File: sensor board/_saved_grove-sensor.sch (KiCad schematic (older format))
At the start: 28 parts, among them P1 CONN_01X03, P2 CONN_01X03, P3 CONN_01X03, P4 CONN_01X04, Q1 PN2222A, U1 ADD8704, U2 SI1143, U3 Teensy_3.1

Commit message: Drew some footprints and PCB outline
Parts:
- C1, C2, C3: footprint (none) -> Capacitors_SMD:C_0603_HandSoldering
- D1, D2, D3: footprint (none) -> LEDs:LED-5MM
- P1, P2, P3: footprint (none) -> Pin_Headers:Pin_Header_Straight_1x03
- P4: footprint (none) -> Pin_Headers:Pin_Header_Straight_1x04
- Q1: footprint (none) -> TO_SOT_Packages_THT:TO-92_Horizontal1_Inline_Narrow_Oval
- R1, R10, R11, R12, R13, R14, R3, R4, R6, R7, R8, R9: footprint (none) -> Resistors_SMD:R_0603_HandSoldering
- R2, R5: footprint (none) -> Resistors_SMD:R_0402
- U2: footprint (none) -> SI1143:SI1143

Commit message: Added sensor mounting holes
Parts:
- removed P1, P2, P3: CONN_01X03, Pin_Headers:Pin_Header_Straight_1x03, symbol CONN_01X03
- removed P4: CONN_01X04, Pin_Headers:Pin_Header_Straight_1x04, symbol CONN_01X04
- removed Q1: PN2222A, TO_SOT_Packages_THT:TO-92_Horizontal1_Inline_Narrow_Oval, symbol PN2222A
- added C4: 10uF, Capacitors_SMD:C_0603_HandSoldering, symbol C
- added C5, C6: 0.1uF, Capacitors_SMD:C_0603_HandSoldering, symbol C
- added P1, P3, P4, P5, P6, P7, P8, P9: CONN_01X01, Pin_Headers:Pin_Header_Straight_1x01, symbol CONN_01X01
- added P2: CONN_01X06, Pin_Headers:Pin_Header_Straight_1x06, symbol CONN_01X06
- added Q1: Q_NPN_BEC, TO_SOT_Packages_SMD:SOT-23, symbol Q_NPN_BEC
- added R21, R22, R25: 0, Resistors_SMD:R_0603_HandSoldering, symbol R
- added R23, R24, R26: 10k, Resistors_SMD:R_0603_HandSoldering, symbol R
- added U4: MCP1700, TO_SOT_Packages_SMD:SOT-23, symbol MCP1700
- added U5, U6: WS2812B, LEDs:LED_WS2812B-PLCC4, symbol WS2812B
- D1, D2, D3: footprint LEDs:LED-5MM -> LEDs:LED_0805
- R2: footprint Resistors_SMD:R_0402 -> Resistors_SMD:R_0603
- U1: footprint (none) -> SI1143:TSSOP-14
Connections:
- net labels added: LED_IN, PIR_IN
- net labels removed: CS, MISO, MOSI, PROX_INT, RGB1, RGB2
- wire segments 97 -> 131
- no-connect marks 2 -> 22
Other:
- note added: "Connector to main board\n"
- note added: "Mounting holes (M3)\n"
- note removed: "Connector to dispatcher"
- moved on the sheet: R10, R12, R9

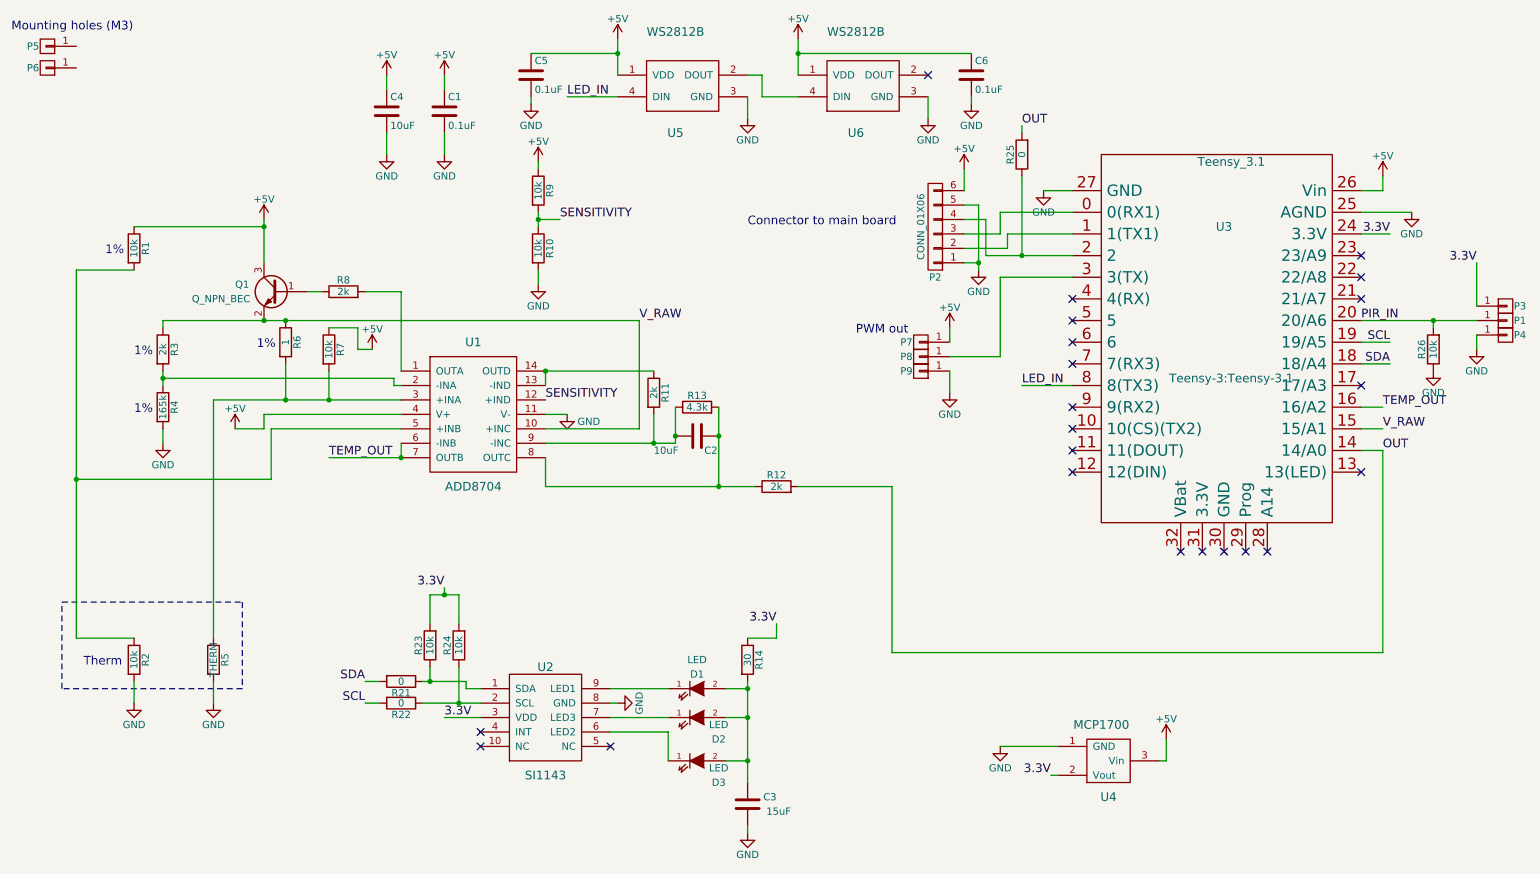
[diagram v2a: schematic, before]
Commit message: Removed old gerbers, added v2
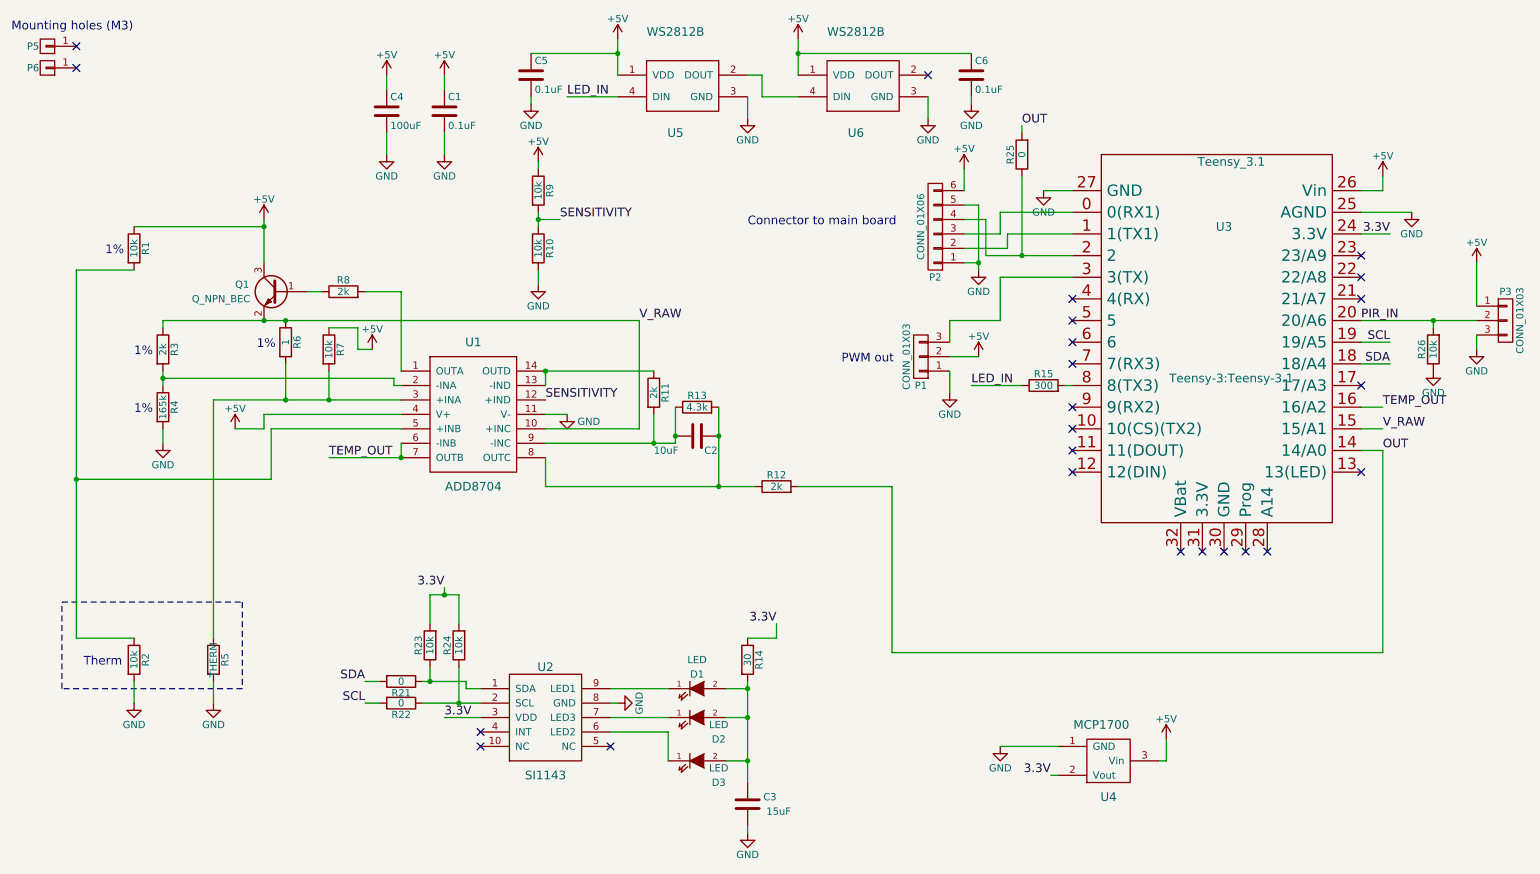
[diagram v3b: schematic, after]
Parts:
- removed P1, P3, P4, P7, P8, P9: CONN_01X01, Pin_Headers:Pin_Header_Straight_1x01, symbol CONN_01X01
- added P1, P3: CONN_01X03, Pin_Headers:Pin_Header_Straight_1x03, symbol CONN_01X03
- added R15: 300, Resistors_SMD:R_0603_HandSoldering, symbol R
- C4: value 10uF -> 100uF; footprint Capacitors_SMD:C_0603_HandSoldering -> Capacitors_SMD:C_1210_HandSoldering
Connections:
- net +5V: now also P1.2 (P2), P3.1 (P1)
- net GND: now also P1.1 (P1), P3.3 (P3)
- net LED_IN: now also R15.1; no longer U3.8 (8(TX3))
- net PIR_IN: now also P3.2 (P2)
- net at U3.3 (3(TX)): now also P1.3 (P3)
- new net: R15.2, U3.8 (8(TX3))
- no-connect marks 22 -> 24
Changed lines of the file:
@@
 L +5V #PWR015
 U 1 1 576C07D7
-P 7100 2700
-F 0 "#PWR015" H 7100 2550 50  0001 C CNN
-F 1 "+5V" H 7100 2840 50  0000 C CNN
-F 2 "" H 7100 2700 50  0000 C CNN
-F 3 "" H 7100 2700 50  0000 C CNN
-	1    7100 2700
+P 7300 2900
+F 0 "#PWR015" H 7300 2750 50  0001 C CNN
+F 1 "+5V" H 7300 3040 50  0000 C CNN
+F 2 "" H 7300 2900 50  0000 C CNN
+F 3 "" H 7300 2900 50  0000 C CNN
+	1    7300 2900
 	1    0    0    -1
 $EndComp
@@
 	1    0    0    -1
 $EndComp
-Text Notes 6450 2750 0    60   ~ 0
+Text Notes 6350 2950 0    60   ~ 0
 PWM out\n
 $Comp
@@
 	1    0    0    -1
 $EndComp
-$Comp
-L CONN_01X01 P7
-U 1 1 576CE696
-P 6900 2800
-F 0 "P7" H 7000 2800 50  0000 C CNN
-F 1 "CONN_01X01" H 7300 2800 50  0001 C CNN
-F 2 "Pin_Headers:Pin_Header_Straight_1x01" H 6900 2800 50  0001 C CNN
-F 3 "" H 6900 2800 50  0000 C CNN
-	1    6900 2800
-	-1   0    0    1
-$EndComp
-$Comp
-L CONN_01X01 P8
-U 1 1 576CE71E
-P 6900 2900
-F 0 "P8" H 7000 2900 50  0000 C CNN
-F 1 "CONN_01X01" H 7300 2900 50  0001 C CNN
-F 2 "Pin_Headers:Pin_Header_Straight_1x01" H 6900 2900 50  0001 C CNN
-F 3 "" H 6900 2900 50  0000 C CNN
-	1    6900 2900
-	-1   0    0    1
-$EndComp
-$Comp
-L CONN_01X01 P9
-U 1 1 576CE79F
-P 6900 3000
-F 0 "P9" H 7000 3000 50  0000 C CNN
-F 1 "CONN_01X01" H 7300 3000 50  0001 C CNN
-F 2 "Pin_Headers:Pin_Header_Straight_1x01" H 6900 3000 50  0001 C CNN
-F 3 "" H 6900 3000 50  0000 C CNN
-	1    6900 3000
-	-1   0    0    1
-$EndComp
 NoConn ~ 3850 5500
 Text Label 9950 2650 0    60   ~ 0
 PIR_IN
-$Comp
-L CONN_01X01 P1
-U 1 1 577554A8
-P 10950 2650
-F 0 "P1" H 11050 2650 50  0000 C CNN
-F 1 "CONN_01X01" V 11050 2650 50  0001 C CNN
-F 2 "Pin_Headers:Pin_Header_Straight_1x01" H 10950 2650 50  0001 C CNN
-F 3 "" H 10950 2650 50  0000 C CNN
-	1    10950 2650
-	1    0    0    -1
-$EndComp
 NoConn ~ 9950 3700
 NoConn ~ 9950 3100
@@
 P 3200 1200
 F 0 "C4" H 3225 1300 50  0000 L CNN
-F 1 "10uF" H 3225 1100 50  0000 L CNN
-F 2 "Capacitors_SMD:C_0603_HandSoldering" H 3238 1050 50  0001 C CNN
+F 1 "100uF" H 3225 1100 50  0000 L CNN
+F 2 "Capacitors_SMD:C_1210_HandSoldering" H 3238 1050 50  0001 C CNN
 F 3 "" H 3200 1200 50  0000 C CNN
 	1    3200 1200
@@
 	1    0    0    -1
 $EndComp
-$Comp
-L CONN_01X01 P3
-U 1 1 577CE261
-P 10950 2550
-F 0 "P3" H 11050 2550 50  0000 C CNN
-F 1 "CONN_01X01" V 11050 2550 50  0001 C CNN
-F 2 "Pin_Headers:Pin_Header_Straight_1x01" H 10950 2550 50  0001 C CNN
-F 3 "" H 10950 2550 50  0000 C CNN
-	1    10950 2550
-	1    0    0    -1
-$EndComp
-$Comp
-L CONN_01X01 P4
-U 1 1 577CE313
-P 10950 2750
-F 0 "P4" H 11050 2750 50  0000 C CNN
-F 1 "CONN_01X01" V 11050 2750 50  0001 C CNN
-F 2 "Pin_Headers:Pin_Header_Straight_1x01" H 10950 2750 50  0001 C CNN
-F 3 "" H 10950 2750 50  0000 C CNN
-	1    10950 2750
-	1    0    0    -1
-$EndComp
-Text Label 10750 2250 2    60   ~ 0
-3.3V
 $Comp
 L GND #PWR023
@@
 	10100 3400 9950 3400
 Wire Wire Line
-	7100 2700 7100 2800
-Wire Wire Line
 	7100 3000 7100 3150
 Wire Wire Line
@@
 Wire Wire Line
 	7950 2350 7450 2350
-Wire Wire Line
-	7450 2350 7450 2900
-Wire Wire Line
-	7450 2900 7100 2900
 Wire Wire Line
 	7200 1950 7350 1950
@@
 	7250 800  6050 800
 Connection ~ 6050 800
-Text Label 7600 3100 0    60   ~ 0
+Text Label 7250 3100 0    60   ~ 0
 LED_IN
 Wire Wire Line
-	7600 3100 7950 3100
+	7900 3100 7950 3100
 NoConn ~ 7950 3250
 NoConn ~ 7950 2950
@@
 Text Notes 600  650  0    60   ~ 0
 Mounting holes (M3)\n
+NoConn ~ 1050 750
+NoConn ~ 1050 900
+$Comp
+L CONN_01X03 P1
+U 1 1 579B74D1
+P 6900 2900
+F 0 "P1" H 6900 3100 50  0000 C CNN
+F 1 "CONN_01X03" V 7000 2900 50  0000 C CNN
+F 2 "Pin_Headers:Pin_Header_Straight_1x03" H 6900 2900 50  0001 C CNN
+F 3 "" H 6900 2900 50  0000 C CNN
+	1    6900 2900
+	-1   0    0    1
+$EndComp
+$Comp
+L CONN_01X03 P3
+U 1 1 579B7592
+P 10950 2650
+F 0 "P3" H 10950 2850 50  0000 C CNN
+F 1 "CONN_01X03" V 11050 2650 50  0000 C CNN
+F 2 "Pin_Headers:Pin_Header_Straight_1x03" H 10950 2650 50  0001 C CNN
+F 3 "" H 10950 2650 50  0000 C CNN
+	1    10950 2650
+	1    0    0    -1
+$EndComp
+$Comp
+L R R15
+U 1 1 579BC9AF
+P 7750 3100
+F 0 "R15" V 7830 3100 50  0000 C CNN
+F 1 "300" V 7750 3100 50  0000 C CNN
+F 2 "Resistors_SMD:R_0603_HandSoldering" V 7680 3100 50  0001 C CNN
+F 3 "" H 7750 3100 50  0000 C CNN
+	1    7750 3100
+	0    -1   -1   0
+$EndComp
+Wire Wire Line
+	7600 3100 7250 3100
+$Comp
+L +5V #PWR033
+U 1 1 579C073C
+P 10750 2250
+F 0 "#PWR033" H 10750 2100 50  0001 C CNN
+F 1 "+5V" H 10750 2390 50  0000 C CNN
+F 2 "" H 10750 2250 50  0000 C CNN
+F 3 "" H 10750 2250 50  0000 C CNN
+	1    10750 2250
+	1    0    0    -1
+$EndComp
+Wire Wire Line
+	7100 2900 7300 2900
+Wire Wire Line
+	7450 2350 7450 2650
+Wire Wire Line
+	7450 2650 7100 2650
+Wire Wire Line
+	7100 2650 7100 2800
 $EndSCHEMATC
